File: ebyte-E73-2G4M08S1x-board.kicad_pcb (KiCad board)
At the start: 4 copper layers, 26.7 x 47 mm, 39 parts, among them J1 USB_B_Micro, J2 USB_B_Micro, J3 BAT, J4 Conn_01x18_Male, J5 Conn_01x18_Male, J6 Conn_ARM_JTAG_SWD_10, J7 Conn_02x03_Odd_Even, Q1 PMV65XP, SW1 SW_Push, U1 MCP73831-2-OT, U2 LP5907MFX-3.3, U3 CH340E, U4 E73-2G4M08S1E, U5 L3GD20, Y1 Crystal

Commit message: Preliminary PCB layout
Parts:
- C6, C7, R1, Y1: moved to F.Cu
- J1, J2: footprint Connector_USB:USB_Micro-AB_Molex_47590-0001 -> Connector_USB:USB_Micro-B_Amphenol_10103594-0001LF_Horizontal
- moved R2 30.3 mm to (151.0, 110.1)
- moved R3 28.0 mm to (154.4, 107.7)
- moved C1 27.5 mm to (153.5, 110.0), turned to 90 degrees
- moved C3 26.8 mm to (144.7, 109.3), turned to 90 degrees
- moved C5 22.6 mm to (155.1, 105.2), turned to 90 degrees
- moved C2 21.5 mm to (145.7, 101.5)
- moved C10 17.8 mm to (148.1, 73.4), turned to 90 degrees
- moved R5 16.4 mm to (141.2, 91.3), turned to 270 degrees
- moved C4 15.6 mm to (142.2, 100.2)
- moved C9 15.2 mm to (150.7, 73.4), turned to 90 degrees
- moved R4 14.3 mm to (154.4, 109.1)
- moved D6 14.0 mm to (141.2, 88.4), turned to 90 degrees
- moved C8 12.4 mm to (152.1, 79.3), turned to 90 degrees
- moved D4 12.1 mm to (154.4, 107.2)
- moved U5 11.1 mm to (149.2, 80.3)
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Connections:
- Y1 pad 1: Net-(C6-Pad1) -> Net-(C7-Pad1)
- Y1 pad 2: Net-(C7-Pad1) -> Net-(C6-Pad1)
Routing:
- net GND: track 3.88 -> 67.2 mm, vias 2 -> 32
- net SWC: track 0.00 -> 55.6 mm, vias 0 -> 1
- net P0.05: track 0.00 -> 53.9 mm, vias 0 -> 4
- net VBUS: track 21.6 -> 71.2 mm, vias 0 -> 3
- net P0.08: track 0.00 -> 46.2 mm, vias 0 -> 2
- net P0.12: track 0.00 -> 45.0 mm, vias 0 -> 3
- net D+: track 0.00 -> 43.5 mm
- net D-: track 0.00 -> 43.2 mm
- net SWD: track 0.00 -> 43.1 mm, vias 0 -> 1
- net P0.06: track 0.00 -> 41.4 mm, vias 0 -> 2
- net P0.04: track 0.00 -> 35.6 mm, vias 0 -> 2
- net P0.07: track 0.00 -> 35.5 mm, vias 0 -> 2
- net SWO: track 16.9 -> 51.3 mm, vias 1 -> 2
- net RST: track 0.00 -> 32.8 mm, vias 0 -> 3
- net VDDH: track 0.00 -> 31.8 mm, vias 0 -> 3
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- added copper zone on B.Cu, net GND
- added copper zone on F.Cu, net GND

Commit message: Update sch, pcb, bom
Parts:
- removed TP3: TestPoint, TestPoint:TestPoint_Pad_1.0x1.0mm
- removed the U5 at (149.2, 80.3)
- added D6: LED, LED_SMD:LED_0603_1608Metric, F.Cu at (142.2, 88.4)
- added D8: LED, LED_SMD:LED_0603_1608Metric, F.Cu at (140.4, 107.0)
- added R5: 10k, Resistor_SMD:R_0603_1608Metric, F.Cu at (145.1, 91.5)
- added R7: 470R, Resistor_SMD:R_0603_1608Metric, F.Cu at (142.2, 91.4)
- added R8: 470R, Resistor_SMD:R_0603_1608Metric, F.Cu at (140.4, 110.0)
- added SW2: PTS810, Button_Switch_SMD:SW_SPST_PTS810, F.Cu at (142.6, 95.4)
- added U4: L3GD20, Package_LGA:LGA-16_4x4mm_P0.65mm_LayoutBorder4x4y, B.Cu at (149.2, 80.3)
- C3: value 0.1 -> 100n
- J4, J5: moved to B.Cu
- R4: value R -> 470R
- SW1: value SW_Push -> PTS810
- Y1: value Crystal -> 32768
- moved TP1 17.0 mm to (144.8, 89.0)
- moved SW1 14.9 mm to (142.1, 102.7), turned to 0 degrees
- moved D7 12.7 mm to (155.5, 97.9)
- moved Y1 5.10 mm to (154.4, 90.9), turned to 90 degrees
- moved C7 4.64 mm to (148.5, 91.8), turned to 180 degrees
- moved C8 2.16 mm to (148.5, 90.2)
- moved Q1 1.02 mm to (149.8, 107.6)
- moved D4 0.84 mm to (154.7, 106.4), turned to 90 degrees
- moved R4 0.63 mm to (155.1, 109.2)
- moved R6 0.60 mm to (140.6, 91.4)
- moved D5 0.58 mm to (140.6, 88.4)
- moved C4 0.55 mm to (142.2, 99.6)
- moved R2 0.43 mm to (151.4, 110.2)
- moved C2 0.42 mm to (146.1, 101.5)
- moved C3 0.37 mm to (145.1, 109.3)
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- renumbered C8 to C6, C6 to C7, C7 to C8, D6 to D5, D5 to D7, R5 to R6, U4 to U5
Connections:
- C7 pad 1: Net-(C6-Pad1) (its old number) -> Net-(C7-Pad1)
- C8 pad 1: Net-(C7-Pad1) -> Net-(C8-Pad1)
- D7 pad 4: P0.15 -> P0.04
- U3 pad 6: Net-(TP1-Pad1) -> Net-(D8-Pad2)
- U5 pad 11: Net-(C6-Pad1) (its old number) -> Net-(C7-Pad1)
- U5 pad 13: Net-(C7-Pad1) -> Net-(C8-Pad1)
- U5 pad 25: Net-(TP3-Pad1) -> Net-(TP1-Pad1)
- Y1 pad 2: Net-(C6-Pad1) (its old number) -> Net-(C8-Pad1)
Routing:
- net VDD: track 41.5 -> 33.5 mm, vias 7 -> 9
- net P0.12: track 45.0 -> 52.4 mm, vias 3 -> 2
- net Net-(C8-Pad1): track 0.00 -> 6.57 mm
- net Net-(C6-Pad1) (its old number): track 6.08 -> 0.00 mm
- net P0.07: track 35.5 -> 38.6 mm, vias 2 -> 1
- net Net-(D8-Pad2): track 0.00 -> 3.08 mm, vias 0 -> 1
- net SWD: track 43.1 -> 45.7 mm, vias 1 -> 2
- net Net-(D4-Pad2): track 1.88 -> 4.24 mm
- net P0.04: track 35.6 -> 38.0 mm
- net RST: track 32.8 -> 35.0 mm
- net Net-(C7-Pad1): track 6.43 -> 8.66 mm
- net Net-(TP3-Pad1): track 2.11 -> 0.00 mm
- net P0.05: track 53.9 -> 55.8 mm
- net Net-(J1-Pad6): track 25.6 -> 27.5 mm
- net Net-(D4-Pad1): track 3.47 -> 5.23 mm
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- removed copper zone on B.Cu, net GND
- removed copper zone on F.Cu, net GND
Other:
- board text added: "BAT"
- board text added: "CHG"
- board text added: "DCH"
- board text added: "JTAG"
- board text added: "NRF"
- board text added: "P0.04"
- board text added: "P0.12"
- board text added: "P0.13"
- board text added: "P0.15"
- board text added: "P0.18"
- board text added: "P1.11"
- board text added: "RXTX"
- board text added: "SWD"
- board text added: "UART"

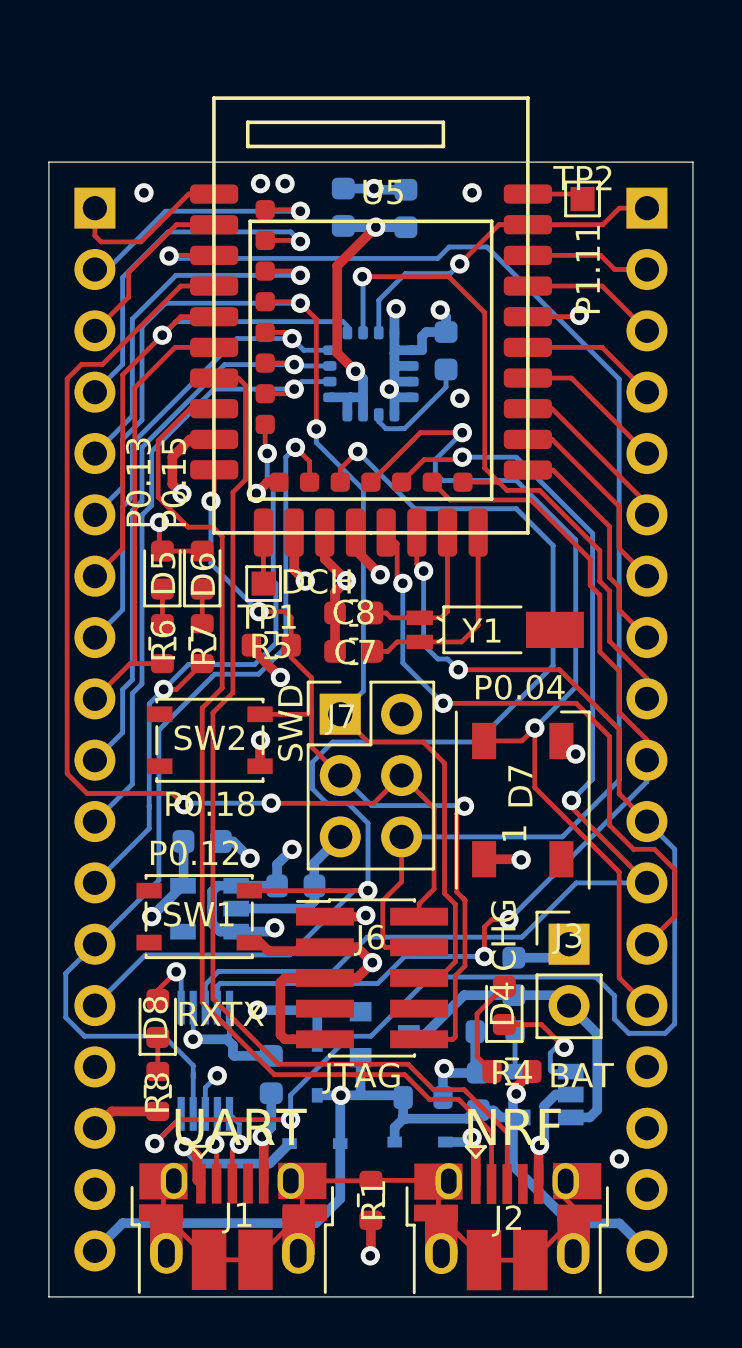
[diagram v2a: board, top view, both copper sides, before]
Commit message: Improve silk
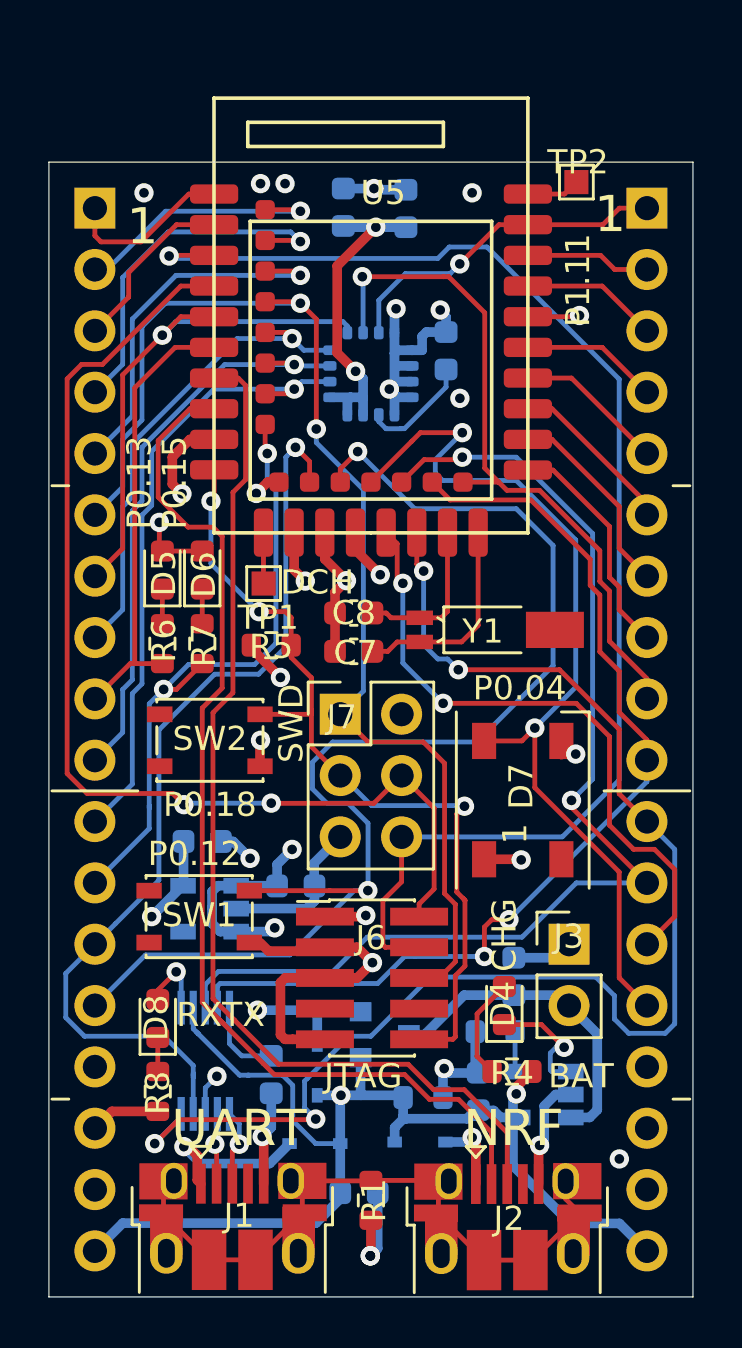
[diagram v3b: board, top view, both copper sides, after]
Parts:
- added C11: 100n, Capacitor_SMD:C_0603_1608Metric, B.Cu at (148.7, 114.2)
- C3: value 100n -> 10n
- moved TP2 0.74 mm to (157.7, 72.3)
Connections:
- net D+ renamed NRF_D+
- net D- renamed NRF_D-
- C3 pad 2: VDD -> Net-(C3-Pad2)
- U3 pad 10: VDD -> Net-(C3-Pad2)
- U3 pad 7: VDD -> VBUS
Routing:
- net VBUS: track 70.0 -> 80.0 mm
- net VDD: track 33.5 -> 27.5 mm, vias 9 -> 8
- net Net-(C3-Pad2): track 0.00 -> 3.43 mm
- net GND: track 67.3 -> 70.0 mm, vias 22 -> 23
- net P0.05: track 55.8 -> 56.8 mm
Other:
- board text added: "1"
- board text added: "JLCJLCJLCJLC"
- board text added: "github.com/dimka-rs/ ebyte-E73-2G4M08S1x -board"

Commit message: Fix module footprint, rework PCB
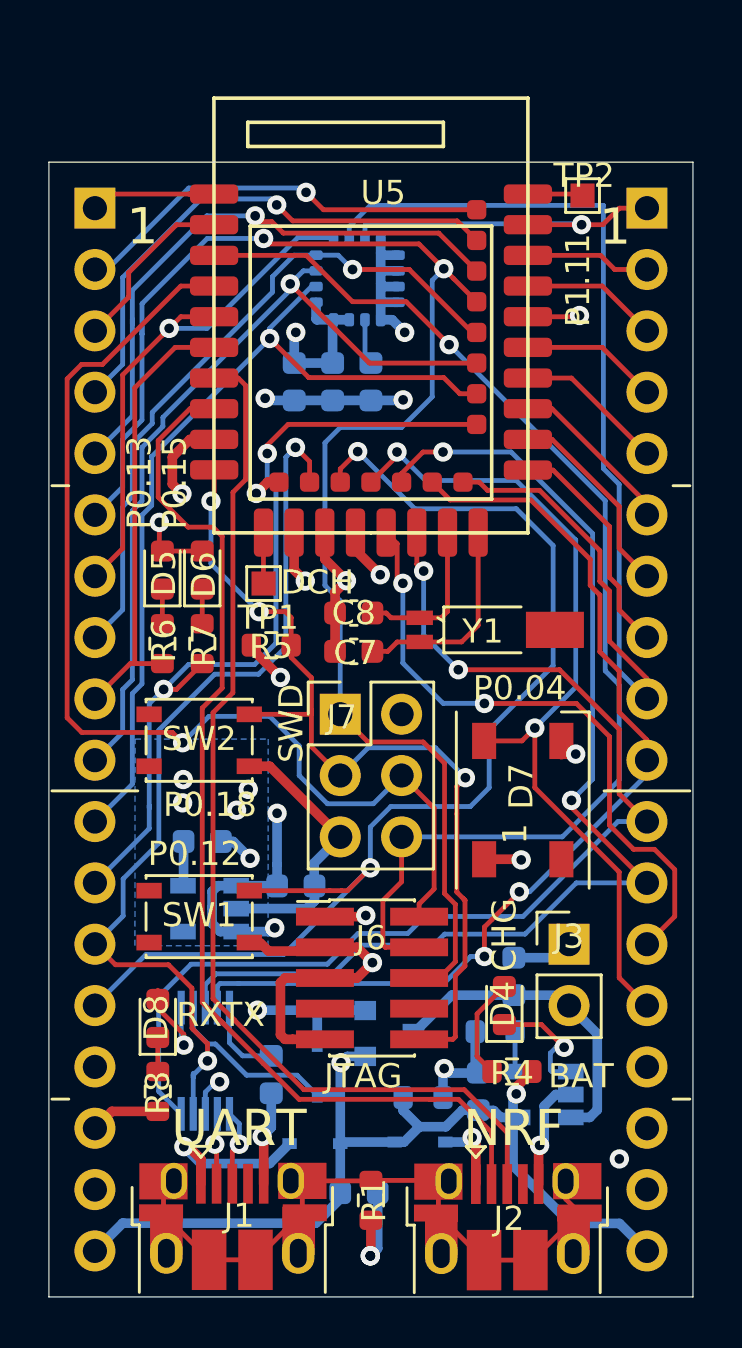
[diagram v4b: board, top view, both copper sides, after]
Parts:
- moved C9 7.79 mm to (147.6, 80.6), turned to 270 degrees
- moved C10 7.51 mm to (146.1, 80.6), turned to 270 degrees
- moved U4 3.98 mm to (148.7, 76.3)
- moved C6 3.37 mm to (149.2, 80.6), turned to 270 degrees
- moved TP2 0.61 mm to (158.0, 72.9)
- moved SW2 0.44 mm to (142.1, 95.4)
- moved Q1 0.20 mm to (150.0, 107.6)
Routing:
- net P0.26: track 29.8 -> 47.1 mm, vias 1 -> 0
- net SWO: track 51.3 -> 64.1 mm
- net P0.05: track 56.8 -> 46.8 mm, vias 4 -> 2
- net P0.17: track 26.2 -> 35.8 mm
- net P0.20: track 24.2 -> 33.4 mm
- net P1.02: track 15.3 -> 24.1 mm
- net VDD: track 27.5 -> 18.7 mm, vias 8 -> 10
- net P0.15: track 26.2 -> 34.4 mm
- net P0.22: track 20.1 -> 28.1 mm
- net SWC: track 55.9 -> 48.5 mm
- net P1.04: track 14.9 -> 21.9 mm
- net P1.06: track 10.9 -> 17.6 mm
- net P0.12: track 52.4 -> 48.4 mm
- net GND: track 70.0 -> 73.4 mm, vias 23 -> 16
- net P0.04: track 38.0 -> 34.8 mm
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- added copper zone on B.Cu, net VDD
